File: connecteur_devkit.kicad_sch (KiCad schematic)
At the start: 8 parts, among them J10 OLED_SPI_2x8, J5 DEVKIT_C2000_ROW_A, J6 DEVKIT_C2000_ROW_B, J7 ESP32_C6_DEVKITC_1_J1, J8 ESP32_C6_DEVKITC_1_J3, U4 ER-OLEDM032-1

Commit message: Ajoute le filtre EMC FL3/FL4 (U3), corrige les caps de sortie 100uF et le rendu 3D du devkit/NCM3S1205MC
- dc.kicad_sch : ajoute FL3/FL4 (Bourns SRF0905) sur le filtre EMC de
  U3, empreinte lib:Filter_Bourns_SRF0905_6.0x9.2mm_My
- connecteur_devkit.kicad_sch : C36/C37 renommes C59/C60, passent en
  100uF 50V / CP_Elec_8x10.5 (electrolytique) au lieu du MLCC 1210 ;
  embases devkit en PinSocket (femelle) au lieu de PinHeader
- connecteurs_nappe/protection_nappe.kicad_sch : complete les labels
  nappe manquants (Discharge, PWM3_B, PWM4_B, Stage2_EN)
- lib/ER-OLEDM032-1.kicad_mod, lib/NCM3S1205MC.kicad_mod : corrige
  l'orientation/offset des modeles 3D (STEP mal aligne)
- lib/DLW5BSZ801TQ2L.step : nouveau modele 3D
- shield.kicad_pcb/.kicad_pro : presets de piste/via supplementaires,
  remove_islands actif
- README.md + doc/shield.png : ajoute le rendu 3D de la carte

Verification avant commit : kicad-cli sch erc (233 violations, 35
erreurs) et pcb drc (329 violations + 183 non connectes) --
inchange dans sa nature par rapport aux sessions precedentes, rien
corrige ici qui ne decoule pas des changements ci-dessus (regle
KICAD.md : rapporter, pas corriger d'office).

Co-Authored-By: Claude Sonnet 5 <noreply@anthropic.com>
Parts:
- removed C36, C37: 100uF, Capacitor_SMD:C_1210_3225Metric, symbol Device:C_Polarized
- added C59, C60: 100uF 50V, Capacitor_SMD:CP_Elec_8x10.5, symbol Device:C_Polarized
- J5, J6: footprint Connector_PinHeader_2.54mm:PinHeader_1x28_P2.54mm_Vertical -> Connector_PinSocket_2.54mm:PinSocket_1x28_P2.54mm_Vertical
- J7, J8: footprint Connector_PinHeader_2.54mm:PinHeader_1x16_P2.54mm_Vertical -> Connector_PinSocket_2.54mm:PinSocket_1x16_P2.54mm_Vertical
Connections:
- net 5V_C2000: now also C60.1
- net 5V_ESP32: now also C59.1
- net GND: now also C59.2, C60.2
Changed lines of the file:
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@@
 		(in_pos_files yes)
 		(dnp no)
-		(property "Reference" "C36"
+		(property "Reference" "C60"
 			(at 98.838 110.998 0)
 			(show_name no)
@@
 			)
 		)
-		(property "Value" "100uF"
+		(property "Value" "100uF 50V"
 			(at 102.838 110.998 0)
 			(show_name no)
@@
 			)
 		)
-		(property "Footprint" "Capacitor_SMD:C_1210_3225Metric"
+		(property "Footprint" "Capacitor_SMD:CP_Elec_8x10.5"
 			(at 100.838 110.998 0)
 			(hide yes)
@@
 			(project "shield"
 				(path "/3e79b37e-13ed-4a43-b954-3b2f3b716c2c/8ca9a22c-ce32-47b8-9bd4-8f1e44cb7b31"
-					(reference "C36")
+					(reference "C60")
 					(unit 1)
 				)
@@
 		(in_pos_files yes)
 		(dnp no)
-		(property "Reference" "C37"
+		(property "Reference" "C59"
 			(at 337.852 83.058 0)
 			(show_name no)
@@
 			)
 		)
-		(property "Value" "100uF"
+		(property "Value" "100uF 50V"
 			(at 341.852 83.058 0)
 			(show_name no)
@@
 			)
 		)
-		(property "Footprint" "Capacitor_SMD:C_1210_3225Metric"
+		(property "Footprint" "Capacitor_SMD:CP_Elec_8x10.5"
 			(at 339.852 83.058 0)
 			(hide yes)
@@
 			(project "shield"
 				(path "/3e79b37e-13ed-4a43-b954-3b2f3b716c2c/8ca9a22c-ce32-47b8-9bd4-8f1e44cb7b31"
-					(reference "C37")
+					(reference "C59")
 					(unit 1)
 				)
@@
 			)
 		)
-		(property "Footprint" "Connector_PinHeader_2.54mm:PinHeader_1x28_P2.54mm_Vertical"
+		(property "Footprint" "Connector_PinSocket_2.54mm:PinSocket_1x28_P2.54mm_Vertical"
 			(at 61.468 102.362 0)
 			(show_name no)
@@
 			)
 		)
-		(property "Footprint" "Connector_PinHeader_2.54mm:PinHeader_1x16_P2.54mm_Vertical"
+		(property "Footprint" "Connector_PinSocket_2.54mm:PinSocket_1x16_P2.54mm_Vertical"
 			(at 374.396 16.51 0)
 			(show_name no)
@@
 			)
 		)
-		(property "Footprint" "Connector_PinHeader_2.54mm:PinHeader_1x16_P2.54mm_Vertical"
+		(property "Footprint" "Connector_PinSocket_2.54mm:PinSocket_1x16_P2.54mm_Vertical"
 			(at 374.396 151.384 0)
 			(show_name no)
@@
 			)
 		)
-		(property "Footprint" "Connector_PinHeader_2.54mm:PinHeader_1x28_P2.54mm_Vertical"
+		(property "Footprint" "Connector_PinSocket_2.54mm:PinSocket_1x28_P2.54mm_Vertical"
 			(at 70.104 193.04 0)
 			(show_name no)

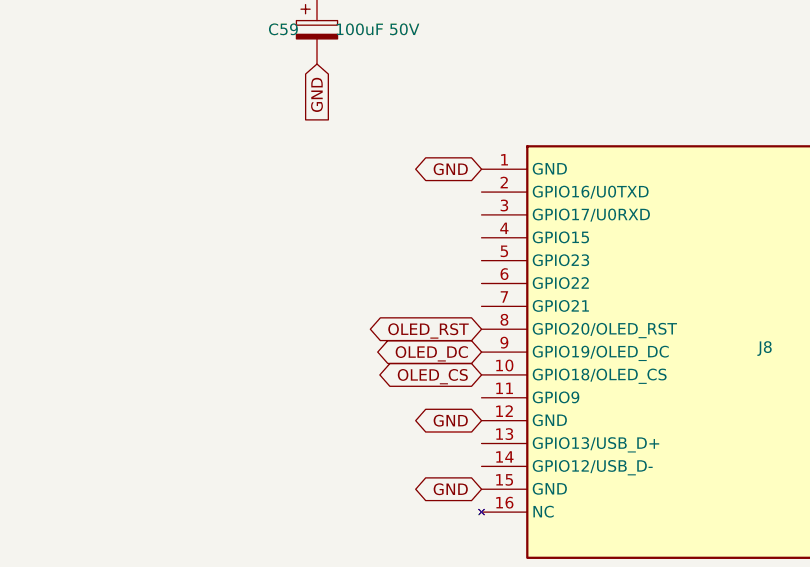
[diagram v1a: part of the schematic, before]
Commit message: Ajoute l'alimentation USB-C Power Delivery des cartes filles (STUSB4531QTR)
Nouvelle feuille usb_pd.kicad_sch : recepteur USB-C Wurth 632722100213,
STUSB4531QTR (negociation PD autonome, 100W/20V/5A), MOSFET P
SQJ459EP-T2_GE3 comme unique interrupteur de puissance (pas d'eFuse),
protections TVS, 2 LED de statut, sortie vers les cartes filles en
daisy chain. Supervision I2C par l'ESP32 (GPIO21/22/23), distincte du
bus I2C des nappes qui reste au C2000.

Deuxieme entree d'alimentation, separee du 11-25V existant. HV_EN et
Discharge (nappe GPIO-1) ne sont pas reutilises : le STUSB4531QTR gere
sa propre coupure/decharge en autonome. Decision #23 pour le detail
complet (composants, justifications, bugs trouves et corriges pendant
la verification ERC).

Co-Authored-By: Claude Sonnet 5 <noreply@anthropic.com>
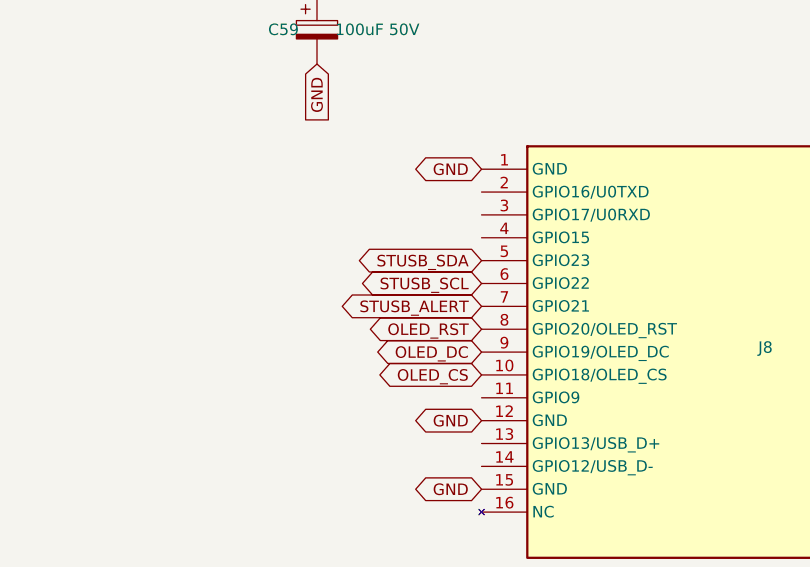
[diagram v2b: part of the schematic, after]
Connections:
- net STUSB_SDA: now reaches J8.5 (GPIO23)
- net STUSB_SCL: now reaches J8.6 (GPIO22)
- net STUSB_ALERT: now reaches J8.7 (GPIO21)
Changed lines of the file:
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@@
+		)
+	)
+	(global_label "STUSB_SDA"
+		(shape bidirectional)
+		(at 358.14 108.712 180)
+		(fields_autoplaced yes)
+		(effects
+			(font
+				(size 1.27 1.27)
+			)
+			(justify right)
+		)
+		(property "Intersheetrefs" "${INTERSHEET_REFS}"
+			(at 358.14 108.712 0)
+			(hide yes)
+			(show_name no)
+			(do_not_autoplace no)
+			(effects
+				(font
+					(size 1.27 1.27)
+				)
+			)
+		)
+	)
+	(global_label "STUSB_SCL"
+		(shape bidirectional)
+		(at 358.14 111.252 180)
+		(fields_autoplaced yes)
+		(effects
+			(font
+				(size 1.27 1.27)
+			)
+			(justify right)
+		)
+		(property "Intersheetrefs" "${INTERSHEET_REFS}"
+			(at 358.14 111.252 0)
+			(hide yes)
+			(show_name no)
+			(do_not_autoplace no)
+			(effects
+				(font
+					(size 1.27 1.27)
+				)
+			)
+		)
+	)
+	(global_label "STUSB_ALERT"
+		(shape bidirectional)
+		(at 358.14 113.792 180)
+		(fields_autoplaced yes)
+		(effects
+			(font
+				(size 1.27 1.27)
+			)
+			(justify right)
+		)
+		(property "Intersheetrefs" "${INTERSHEET_REFS}"
+			(at 358.14 113.792 0)
+			(hide yes)
+			(show_name no)
+			(do_not_autoplace no)
+			(effects
+				(font
+					(size 1.27 1.27)
+				)
+			)
 		)
 	)
